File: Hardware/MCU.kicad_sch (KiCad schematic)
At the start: 24 parts, among them J16 HC-05 Breakout Board, J4 TEENSY_4.1, SW3 SW_Push, SW4 SW_Push

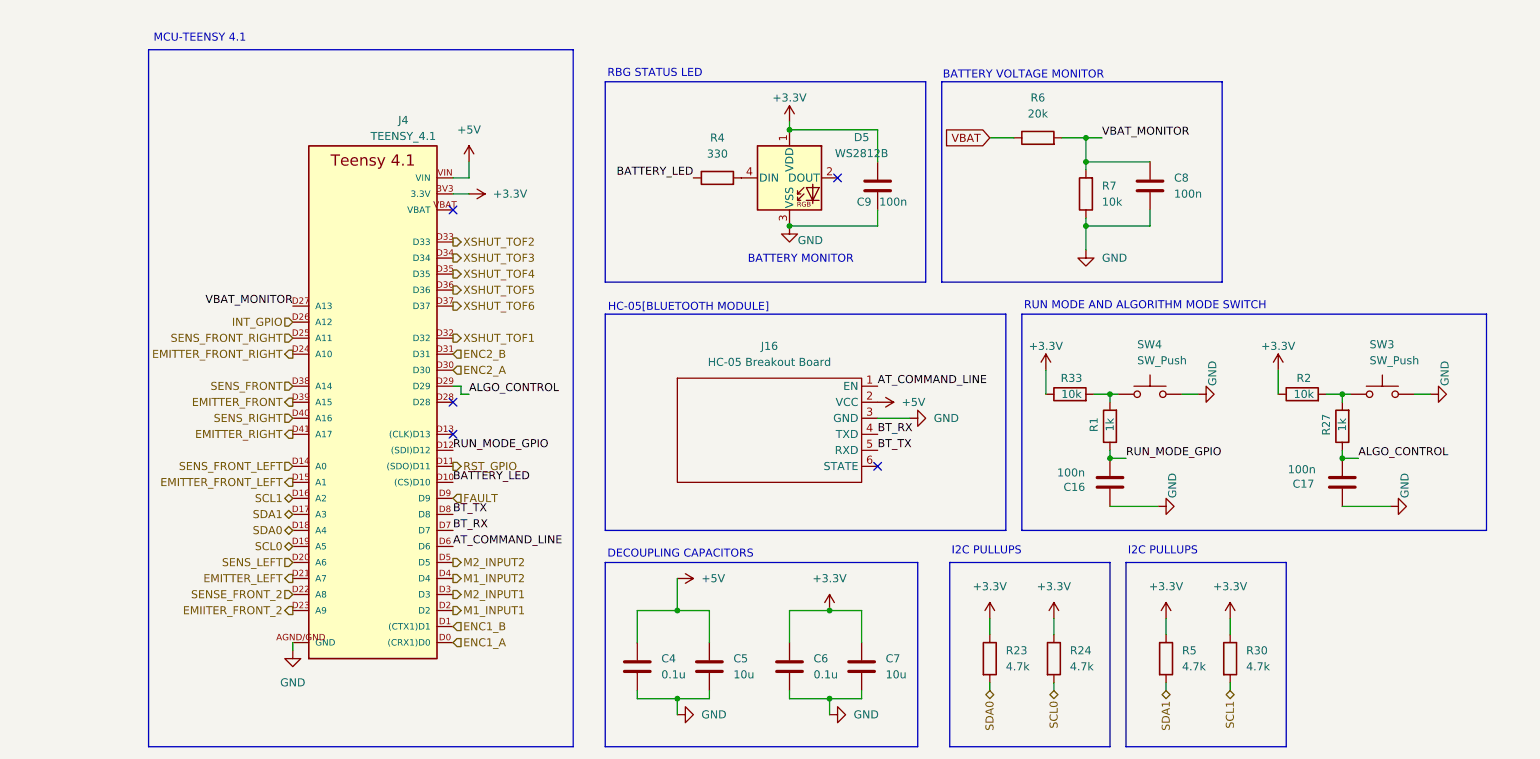
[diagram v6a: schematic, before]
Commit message: Ignore KiCad .history folder
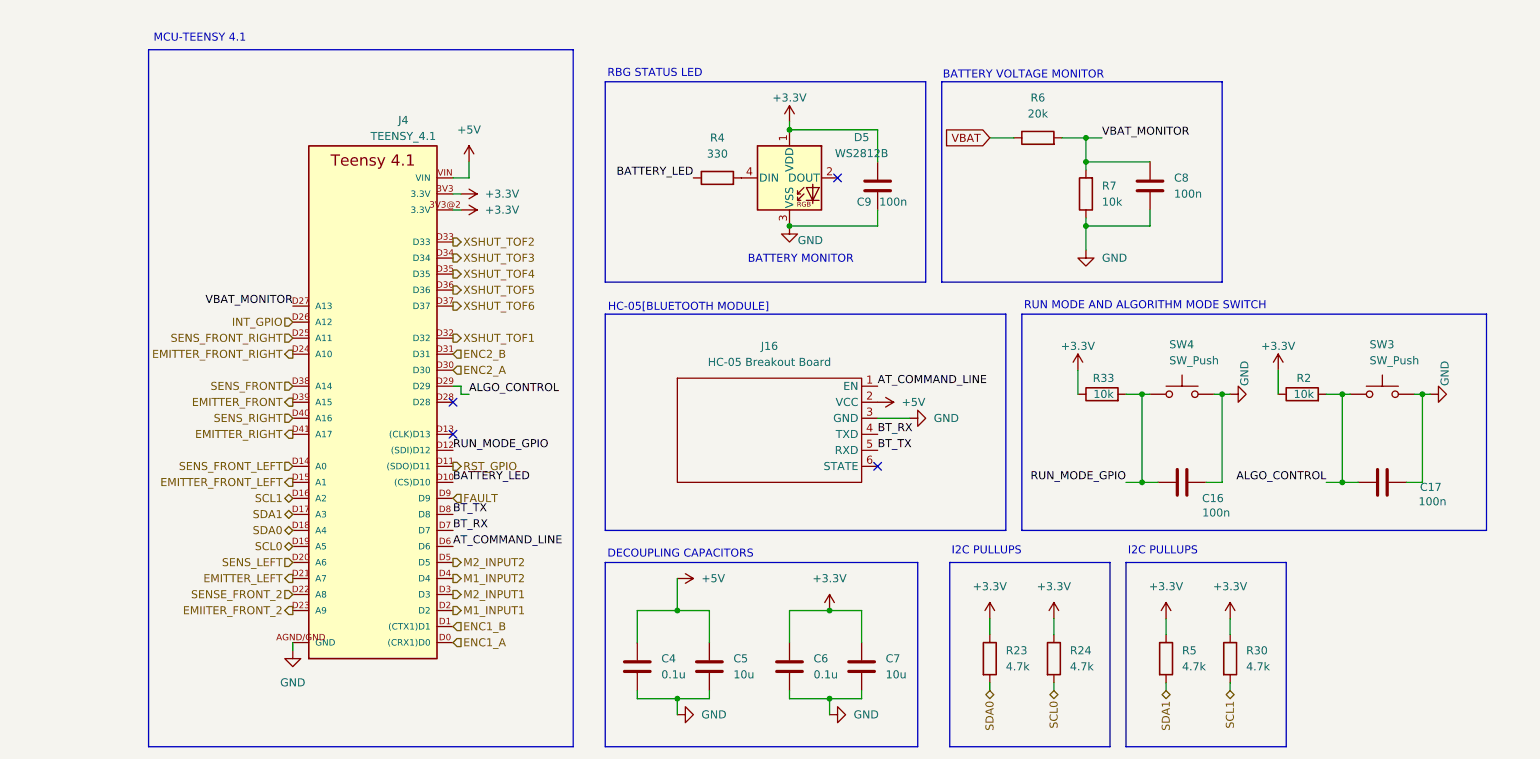
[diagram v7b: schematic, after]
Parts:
- removed R1, R27: 1k, Resistor_SMD:R_0603_1608Metric_Pad0.98x0.95mm_HandSolder, symbol Device:R
- SW3, SW4: footprint Button_Switch_THT:SW_PUSH_6mm_H5mm -> Micromouse:Rectangular Tact Button
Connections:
- net +3.3V: no longer J4.3V3@3 (3.3V)
- net ALGO_CONTROL: now also C17.2, R2.2, SW3.1; no longer C17.1
- net GND: now also C16.1, C17.1; no longer C16.2, C17.2
- net RUN_MODE_GPIO: now also C16.2, R33.2, SW4.1; no longer C16.1
- no-connect marks 5 -> 4
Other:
- moved on the sheet: C16, C17, R33, SW4

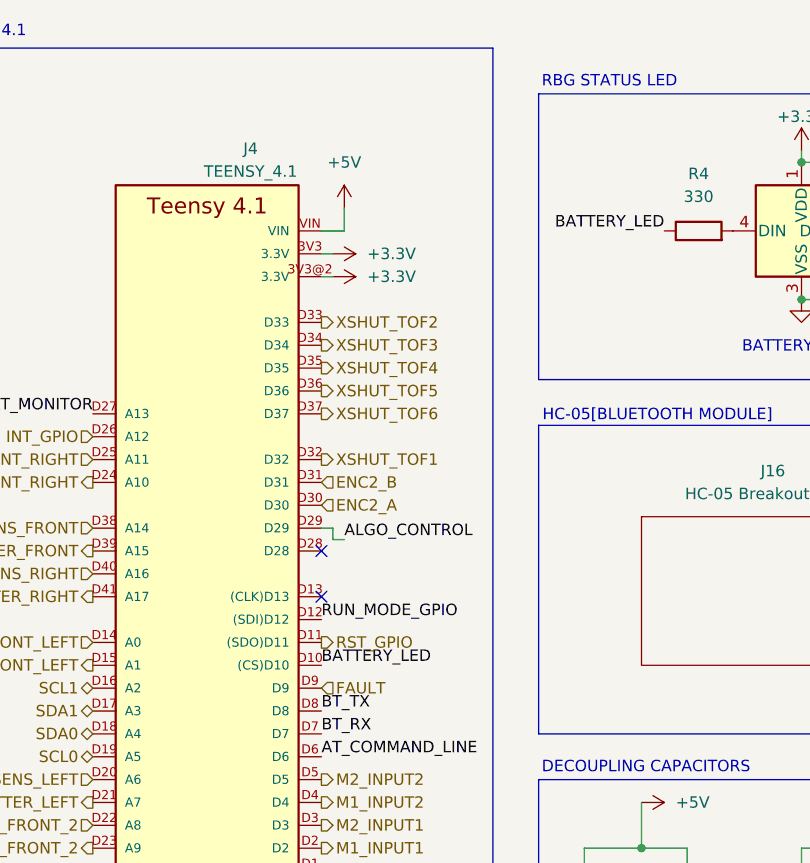
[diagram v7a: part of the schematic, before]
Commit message: updated the dimensiosn of tb6612,shifted placements based on dfm check, other changes
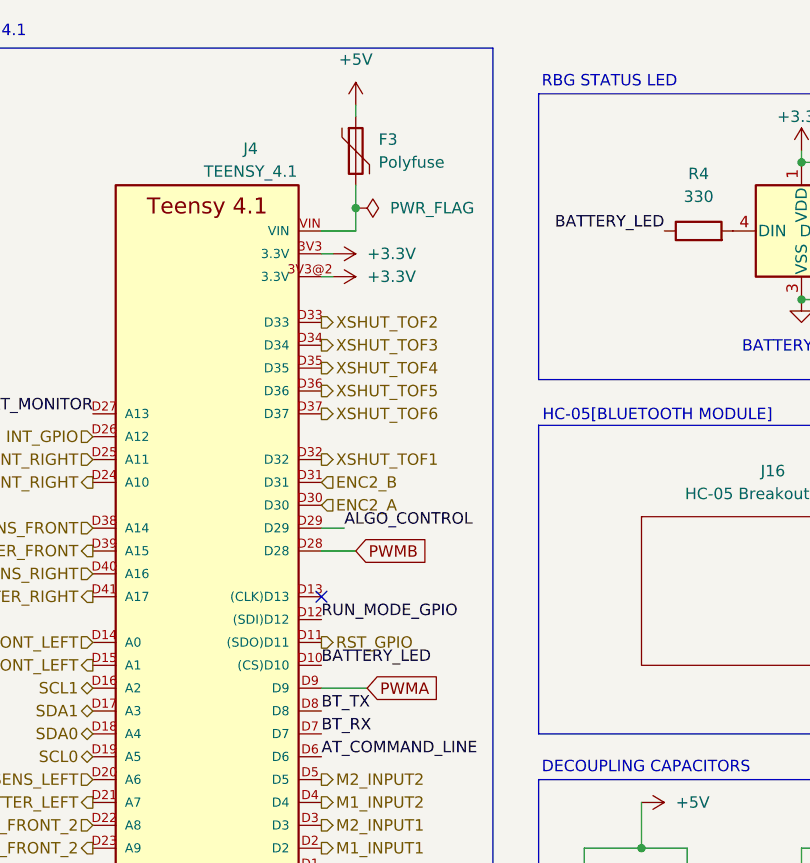
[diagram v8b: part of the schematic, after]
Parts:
- added F3: Polyfuse, Fuse:Fuse_1812_4532Metric_Pad1.30x3.40mm_HandSolder, symbol Device:Polyfuse
- C5, C7: footprint Capacitor_SMD:C_0603_1608Metric_Pad1.08x0.95mm_HandSolder -> Capacitor_SMD:C_1210_3225Metric_Pad1.33x2.70mm_HandSolder
- R4: footprint Resistor_SMD:R_0603_1608Metric_Pad0.98x0.95mm_HandSolder -> Resistor_THT:R_Axial_DIN0414_L11.9mm_D4.5mm_P15.24mm_Horizontal
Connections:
- net +5V: now also F3.1; no longer J4.VIN
- net PWMB: now reaches J4.D28
- net FAULT renamed PWMA
- new net: F3.2, J4.VIN
- no-connect marks 4 -> 3
